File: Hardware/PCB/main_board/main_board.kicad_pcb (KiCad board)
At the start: 2 copper layers, 170 x 170 mm, 67 parts, among them J1 SWD, J2 USB_A, J3 DIN-5_180degree, J4 USB_B, J5 Conn_Coaxial, J6 AudioJack3, Q1 BC547, U1 MCP6002-xSN, U2 NUCLEO-F446RE, U3 6N137

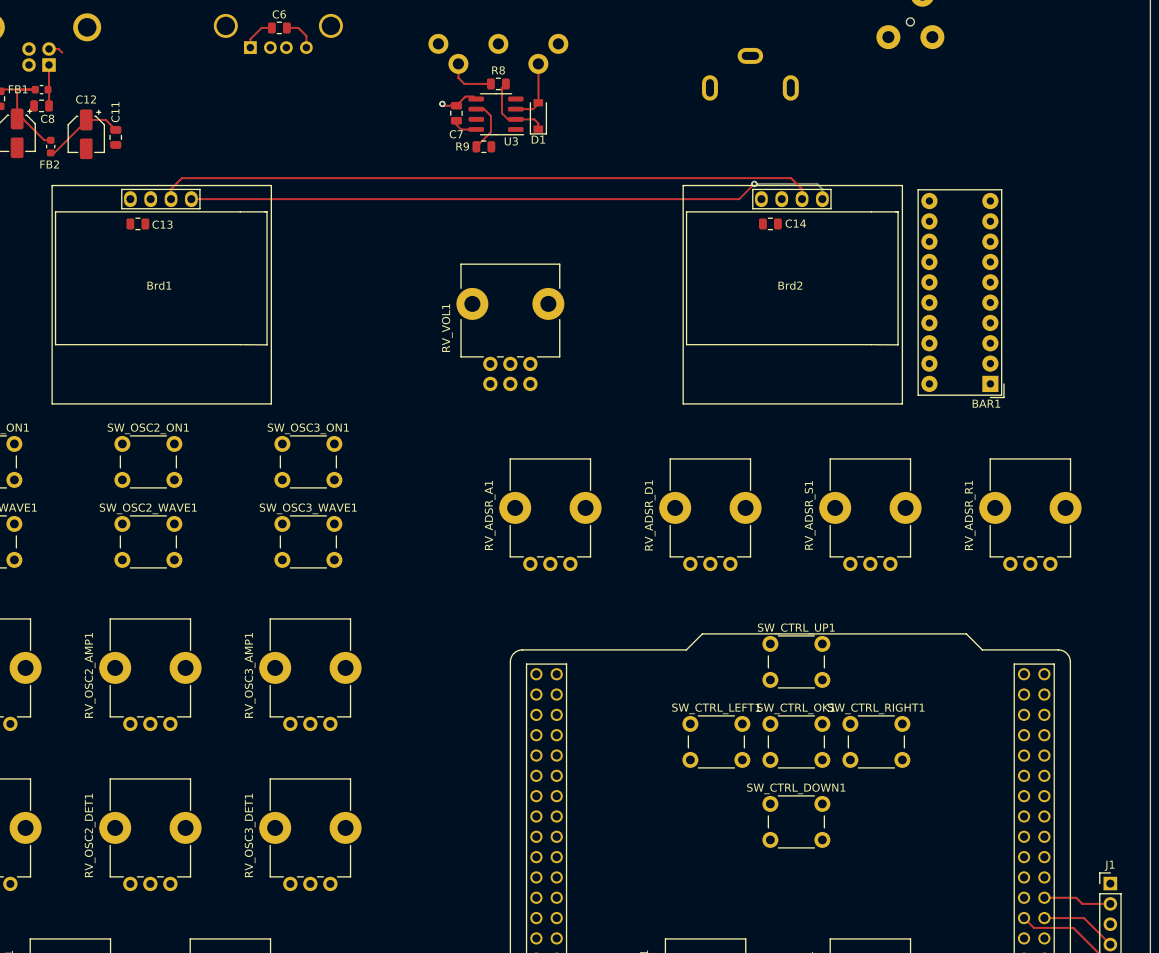
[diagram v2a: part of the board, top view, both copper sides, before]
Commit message: Update 3D view
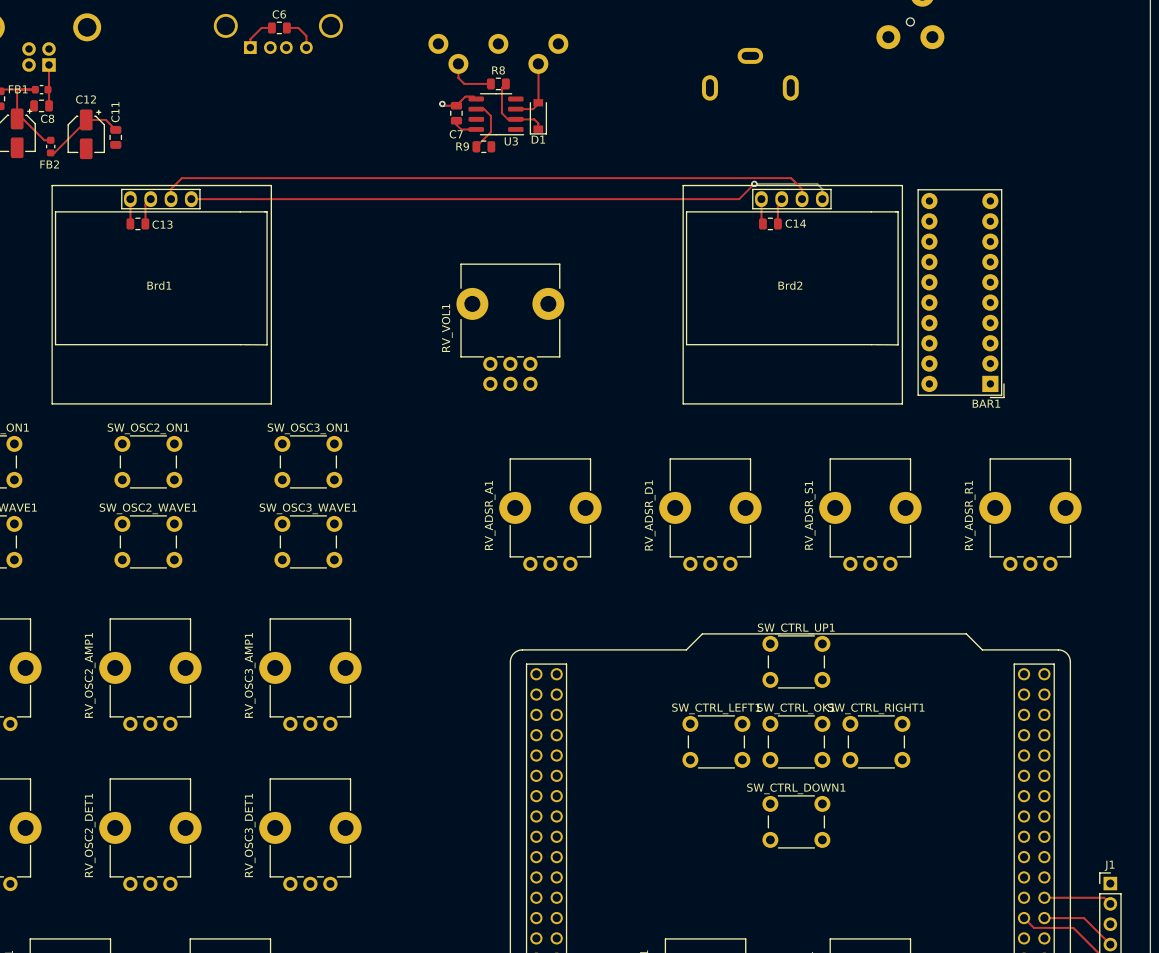
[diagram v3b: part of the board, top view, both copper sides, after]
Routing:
- net +5V: track 23.4 -> 30.1 mm
- net GND: track 22.1 -> 26.2 mm
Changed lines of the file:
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@@
     (thickness 1.6)
     (drawings 1)
-    (tracks 159)
+    (tracks 163)
     (zones 0)
     (modules 67)
@@
     (pad "" np_thru_hole circle (at 4 0 270) (size 1 1) (drill 1) (layers *.Cu *.Mask))
     (pad "" np_thru_hole circle (at 11.5 0 270) (size 1 1) (drill 1) (layers *.Cu *.Mask))
+    (model ${KIPRJMOD}/3dmodels/plastec_jack.stp
+      (offset (xyz 8 0 0))
+      (scale (xyz 0.85 0.9 0.6))
+      (rotate (xyz 0 0 180))
+    )
   )
   (module lib:MODULE_NUCLEO-F446RE (layer F.Cu)
@@
   (segment (start 72.0575 30.5) (end 73.5 30.5) (width 0.25) (layer F.Cu) (net 7))
   (segment (start 73.5 30.5) (end 74.5 31.5) (width 0.25) (layer F.Cu) (net 7))
-  (segment (start 43.529081 33.135) (end 44 33.605919) (width 0.25) (layer F.Cu) (net 7))
-  (segment (start 42.327 33.135) (end 43.529081 33.135) (width 0.25) (layer F.Cu) (net 7))
+  (segment (start 131.38 51.9) (end 131.38 54.8175) (width 0.25) (layer F.Cu) (net 7))
+  (segment (start 52.5 53.5) (end 52.5 55) (width 0.25) (layer F.Cu) (net 7))
+  (segment (start 52.5 51.9) (end 52.5 53.5) (width 0.25) (layer F.Cu) (net 7))
   (segment (start 89.176473 174.275027) (end 89.662 173.7895) (width 0.25) (layer F.Cu) (net 8))
   (segment (start 45 177.5) (end 47.5 180) (width 0.25) (layer F.Cu) (net 8))
@@
   (segment (start 171.69 141.77) (end 175 145.08) (width 0.25) (layer F.Cu) (net 71))
   (segment (start 166.75 141.77) (end 171.69 141.77) (width 0.25) (layer F.Cu) (net 71))
-  (segment (start 175 140) (end 171.5 140) (width 0.25) (layer F.Cu) (net 72))
-  (segment (start 170.73 139.23) (end 166.75 139.23) (width 0.25) (layer F.Cu) (net 72))
-  (segment (start 171.5 140) (end 170.73 139.23) (width 0.25) (layer F.Cu) (net 72))
+  (segment (start 174.23 139.23) (end 166.75 139.23) (width 0.25) (layer F.Cu) (net 72))
+  (segment (start 175 140) (end 174.23 139.23) (width 0.25) (layer F.Cu) (net 72))
   (segment (start 38.35 41.876) (end 38.35 38.215) (width 0.25) (layer F.Cu) (net 76))
   (segment (start 38.35 38.215) (end 40.6105 38.215) (width 0.25) (layer F.Cu) (net 76))
@@
   (segment (start 67.5 31.91) (end 68.91 30.5) (width 0.25) (layer F.Cu) (net 76))
   (segment (start 67.5 32.96) (end 67.5 31.91) (width 0.25) (layer F.Cu) (net 76))
+  (segment (start 133.4375 52.3825) (end 133.92 51.9) (width 0.25) (layer F.Cu) (net 76))
+  (segment (start 133.4375 55) (end 133.4375 52.3825) (width 0.25) (layer F.Cu) (net 76))
+  (segment (start 54.375 52.565) (end 55.04 51.9) (width 0.25) (layer F.Cu) (net 76))
+  (segment (start 54.375 55) (end 54.375 52.565) (width 0.25) (layer F.Cu) (net 76))
   (segment (start 103.5 34.99936) (end 103.49744 34.9968) (width 0.25) (layer F.Cu) (net 77))
   (segment (start 103.5 39.85) (end 103.5 34.99936) (width 0.25) (layer F.Cu) (net 77))

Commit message: Route GPIO
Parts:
- moved RV_LFO_RATE1 153.6 mm to (-83.1, 187.5)
- moved J1 148.8 mm to (28.0, 160.4)
- moved SW_CTRL_DOWN1 133.9 mm to (2.00, 157.5)
- moved SW_CTRL_LEFT1 133.9 mm to (-8.00, 147.5)
- moved SW_CTRL_OK1 133.9 mm to (2.00, 147.5)
- moved SW_CTRL_RIGHT1 133.9 mm to (12.0, 147.5)
- moved SW_CTRL_UP1 133.9 mm to (2.00, 137.5)
- moved BAR1 133.4 mm to (30.0, 105.0)
- moved Brd1 133.4 mm to (-73.9, 92.5)
- moved Brd2 133.4 mm to (5.00, 92.5)
- moved C1 133.4 mm to (-41.1, 194.2)
- moved C10 133.4 mm to (-91.7, 73.7)
- moved C11 133.4 mm to (-79.3, 74.2)
- moved C12 133.4 mm to (-83.0, 73.8)
- moved C13 133.4 mm to (-76.6, 85.0)
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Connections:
- net Net-(J4-Pad2) renamed /power/USB_B_D-
- net Net-(J4-Pad3) renamed /power/USB_B_D+
- net Net-(U2-PadCN10_16) renamed /MCU/MIDI_USB_VBUS
- net Net-(U2-PadCN10_21) renamed /MCU/MIDI_UART_TX
- J6 pad T: Net-(J6-PadT) -> Net-(J6-PadR)
- RV_ADSR_A1 pad 2: /HMI/ADSR_pot_A -> /MCU/ADC1_IN11
- RV_ADSR_D1 pad 2: /HMI/ADSR_pot_D -> /MCU/ADC1_IN10
- RV_ADSR_R1 pad 2: /HMI/ADSR_pot_R -> /MCU/ADC1_IN12
- RV_ADSR_S1 pad 2: /HMI/ADSR_pot_S -> /MCU/ADC1_IN13
- RV_LFO_DEPTH1 pad 2: /HMI/LFO_pot_DEPTH -> /MCU/ADC1_IN15
- RV_LFO_RATE1 pad 2: /HMI/LFO_pot_RATE -> /MCU/ADC1_IN6
- RV_OSC1_AMP1 pad 2: /HMI/OSC1_AMP -> /MCU/ADC1_IN2
- RV_OSC1_DET1 pad 2: /HMI/OSC1_DET -> /MCU/ADC1_IN14
- RV_OSC2_AMP1 pad 2: /HMI/OSC2_AMP -> /MCU/ADC1_IN3
- RV_OSC2_DET1 pad 2: /HMI/OSC2_DET -> /MCU/ADC1_IN9
- RV_OSC3_AMP1 pad 2: /HMI/OSC3_AMP -> /MCU/ADC1_IN8
- RV_OSC3_DET1 pad 2: /HMI/OSC3_DET -> /MCU/ADC1_IN7
- SW_CTRL_OK1 pad 2: /HMI/OSC2_OK -> /MCU/GPIO_PC15
- SW_OSC1_ON1 pad 2: /HMI/OSC1_ON -> /MCU/GPIO_PB4
- SW_OSC1_WAVE1 pad 2: /HMI/OSC1_WAVE -> /MCU/GPIO_PB14
- SW_OSC2_ON1 pad 2: /HMI/OSC2_ON -> /MCU/GPIO_PB15
- SW_OSC2_WAVE1 pad 2: /HMI/OSC2_WAVE -> /MCU/GPIO_PB5
- SW_OSC3_ON1 pad 2: /HMI/OSC3_ON -> /MCU/GPIO_PB10
- SW_OSC3_WAVE1 pad 2: /HMI/OSC3_WAVE -> /MCU/GPIO_PB13
- U2 pad CN10_12: Net-(U2-PadCN10_12) -> /MIDI/MIDI_USB_D+
- U2 pad CN10_13: Net-(U2-PadCN10_13) -> /MCU/ADC1_IN6
- U2 pad CN10_14: Net-(U2-PadCN10_14) -> /MIDI/MIDI_USB_D-
- U2 pad CN10_15: Net-(U2-PadCN10_15) -> /MCU/ADC1_IN7
- U2 pad CN10_17: Net-(U2-PadCN10_17) -> /HMI/I2C_display_SCL
- U2 pad CN10_24: Net-(U2-PadCN10_24) -> /MCU/ADC1_IN9
- U2 pad CN10_25: Net-(U2-PadCN10_25) -> /MCU/GPIO_PB10
- U2 pad CN10_26: Net-(U2-PadCN10_26) -> /MCU/GPIO_PB15
- U2 pad CN10_27: Net-(U2-PadCN10_27) -> /MCU/GPIO_PB4
- U2 pad CN10_28: Net-(U2-PadCN10_28) -> /MCU/GPIO_PB14
- U2 pad CN10_29: Net-(U2-PadCN10_29) -> /MCU/GPIO_PB5
- U2 pad CN10_30: Net-(U2-PadCN10_30) -> /MCU/GPIO_PB13
- U2 pad CN10_33: Net-(U2-PadCN10_33) -> /MIDI/MIDI_Serial_RX
- U2 pad CN10_34: Net-(U2-PadCN10_34) -> /MCU/ADC1_IN14
- U2 pad CN10_35: Net-(U2-PadCN10_35) -> /MCU/ADC1_IN2
- U2 pad CN10_37: Net-(U2-PadCN10_37) -> /MCU/ADC1_IN3
- U2 pad CN10_6: Net-(U2-PadCN10_6) -> /MCU/ADC1_IN15
- U2 pad CN7_21: Net-(U2-PadCN7_21) -> /HMI/I2C_display_SDA
- U2 pad CN7_23: Net-(U2-PadCN7_23) -> /HMI/CTRL_DOWN
- U2 pad CN7_25: Net-(U2-PadCN7_25) -> /HMI/CTRL_RIGHT
- U2 pad CN7_27: Net-(U2-PadCN7_27) -> /MCU/GPIO_PC15
- U2 pad CN7_28: Net-(U2-PadCN7_28) -> /HMI/CTRL_LEFT
- U2 pad CN7_30: Net-(U2-PadCN7_30) -> /HMI/CTRL_UP
- U2 pad CN7_34: Net-(U2-PadCN7_34) -> /MCU/ADC1_IN8
- U2 pad CN7_35: Net-(U2-PadCN7_35) -> /MCU/ADC1_IN12
- U2 pad CN7_36: Net-(U2-PadCN7_36) -> /MCU/ADC1_IN11
- U2 pad CN7_37: Net-(U2-PadCN7_37) -> /MCU/ADC1_IN13
- U2 pad CN7_38: Net-(U2-PadCN7_38) -> /MCU/ADC1_IN10
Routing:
- net /MIDI/MIDI_USB_D-: track 0.00 -> 120.7 mm, vias 0 -> 4
- net /MIDI/MIDI_USB_D+: track 0.00 -> 118.9 mm, vias 0 -> 3
- net /MCU/GPIO_PB4: track 0.00 -> 107.1 mm
- net /MCU/GPIO_PB14: track 0.00 -> 105.7 mm
- net /analogFX/AUDIO_IN: track 0.00 -> 105.6 mm, vias 0 -> 2
- net /HMI/I2C_display_SCL: track 82.5 -> 183.6 mm, vias 0 -> 2
- net /HMI/I2C_display_SDA: track 81.2 -> 178.8 mm
- net /MCU/ADC1_IN8: track 0.00 -> 96.4 mm, vias 0 -> 2
- net /MCU/ADC1_IN14: track 0.00 -> 96.4 mm
- net /MCU/GPIO_PB15: track 0.00 -> 93.2 mm
- net /MIDI/MIDI_Serial_RX: track 0.00 -> 81.0 mm, vias 0 -> 3
- net /MCU/ADC1_IN2: track 0.00 -> 79.1 mm
- net /MCU/GPIO_PB5: track 0.00 -> 79.0 mm
- net /MCU/GPIO_PB10: track 0.00 -> 73.0 mm
- net /MCU/ADC1_IN6: track 0.00 -> 71.8 mm
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
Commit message: Route PWR
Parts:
- added C15: 47p, Capacitor_SMD:C_0805_2012Metric, F.Cu at (101.8, 188.5)
- added C16: 1u, Capacitor_SMD:C_0805_2012Metric, F.Cu at (98.8, 186.0)
- added C17: 51p, Capacitor_SMD:C_0805_2012Metric, F.Cu at (98.8, 192.2)
- added C18: 220n, Capacitor_SMD:C_0805_2012Metric, F.Cu at (93.5, 187.2)
- added C19: 220n, Capacitor_SMD:C_0805_2012Metric, F.Cu at (154.5, 197.2)
- added C20: 100n, Capacitor_SMD:C_0805_2012Metric, F.Cu at (93.2, 195.2)
- added C21: 1u, Capacitor_SMD:C_0805_2012Metric, F.Cu at (87.2, 194.2)
- added D2: 1N4148W, Diode_SMD:D_SOD-123, F.Cu at (101.2, 192.2)
- added D3: 1N4148W, Diode_SMD:D_SOD-123, F.Cu at (104.0, 192.2)
- added G***: LOGO, lib:logo_INSA, F.Cu at (32.8, 203.0)
- added R10: 4.7k, Resistor_SMD:R_0805_2012Metric, F.Cu at (101.8, 186.2)
- added R11: 10k, Resistor_SMD:R_0805_2012Metric, F.Cu at (90.5, 186.0)
- added R12: 10k, Resistor_SMD:R_0805_2012Metric, F.Cu at (96.5, 186.0)
- added R13: 10k, Resistor_SMD:R_0805_2012Metric, F.Cu at (88.2, 186.0)
- added R14: 500, Resistor_SMD:R_0805_2012Metric, F.Cu at (104.8, 187.2)
- added R15: 1k, Resistor_SMD:R_0805_2012Metric, F.Cu at (96.0, 196.0)
- added R16: 220, Resistor_SMD:R_0805_2012Metric, F.Cu at (150.8, 197.2)
- added R17: 10k, Resistor_SMD:R_0805_2012Metric, F.Cu at (93.5, 185.0)
- added R18: 1k, Resistor_SMD:R_0805_2012Metric, F.Cu at (88.0, 191.2)
- added R19: 1k, Resistor_SMD:R_0805_2012Metric, F.Cu at (87.2, 196.5)
- added U4: RC4558, Package_SO:SOIC-8_3.9x4.9mm_P1.27mm, F.Cu at (93.2, 191.2)
- C5: value 4.7u -> 100n
- FB1, FB2: value BLM18pg221sn1d - Ferrite_Bead -> BLM21PG221SH1D - Ferrite_Bead; footprint Inductor_SMD:L_0603_1608Metric -> Inductor_SMD:L_0805_2012Metric
- RV_DIST_DRIVE1: value 10k -> 500k log
- RV_DIST_TONE1: value 10k -> 22k
- moved C8 143.9 mm to (55.2, 75.5), turned to 0 degrees
- moved BAR1 140.4 mm to (170.2, 112.2)
- moved Brd1 140.4 mm to (66.4, 99.8)
- moved Brd2 140.4 mm to (145.2, 99.8)
- moved C1 140.4 mm to (99.2, 201.5)
- moved C10 140.4 mm to (48.6, 80.9)
- moved C13 140.4 mm to (63.7, 92.2)
- moved C14 140.4 mm to (142.8, 92.2)
- moved C2 140.4 mm to (87.7, 208.1)
- moved C3 140.4 mm to (87.7, 211.9)
- moved C4 140.4 mm to (99.2, 203.5)
- moved C5 140.4 mm to (97.9, 209.3)
- moved C6 140.4 mm to (81.4, 67.8)
- moved C7 140.4 mm to (103.5, 78.4)
- moved C9 140.4 mm to (46.3, 76.6)
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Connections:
- net Net-(C8-Pad1) renamed /power/PWR_RAW
- C4 pad 1: /analogFX/AUDIO_OUT -> /analogFX/OUT_VCF__IN_DIST
- RV_DIST_DRIVE1 pad 2: Net-(RV_DIST_DRIVE1-Pad2) -> Net-(C17-Pad1)
- RV_DIST_DRIVE1 pad 3: Net-(RV_DIST_DRIVE1-Pad3) -> Net-(C17-Pad1)
- U2 pad CN10_20: Net-(U2-PadCN10_20) -> GND
- U2 pad CN10_32: Net-(U2-PadCN10_32) -> GND
- U2 pad CN10_9: Net-(U2-PadCN10_20) -> GND
- U2 pad CN7_19: Net-(U2-PadCN7_19) -> GND
- U2 pad CN7_20: Net-(U2-PadCN7_19) -> GND
- U2 pad CN7_22: Net-(U2-PadCN7_19) -> GND
- U2 pad CN7_6: Net-(U2-PadCN7_6) -> +5V
- U2 pad CN7_8: Net-(U2-PadCN7_19) -> GND
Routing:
- net +3V3: track 0.00 -> 299.5 mm, vias 0 -> 2
- net +5V: track 30.1 -> 322.8 mm, vias 0 -> 3
- net +5VA: track 18.9 -> 274.2 mm
- net Net-(C18-Pad1): track 0.00 -> 83.4 mm
- net /MCU/SWO: track 0.00 -> 73.4 mm, vias 0 -> 1
- net Net-(R18-Pad1): track 0.00 -> 66.6 mm, vias 0 -> 2
- net Net-(C17-Pad1): track 0.00 -> 41.6 mm
- net Net-(R14-Pad1): track 0.00 -> 39.3 mm
- net GND: track 26.2 -> 64.7 mm, vias 4 -> 12
- net /analogFX/OUT_VCF__IN_DIST: track 0.00 -> 34.2 mm, vias 0 -> 2
- net Net-(J2-Pad5): track 0.00 -> 16.0 mm
- net Net-(C15-Pad1): track 0.00 -> 13.6 mm
- net Net-(J4-Pad5): track 0.00 -> 12.0 mm
- net Net-(R11-Pad2): track 0.00 -> 10.1 mm
- net Net-(C16-Pad1): track 0.00 -> 8.01 mm
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- added copper zone on B.Cu, net GND
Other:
- net class GND added: clearance 0.2, trace_width 0.4, via_dia 0.9, via_drill 0.45
- net class Power added: clearance 0.2, trace_width 0.5, via_dia 1.2, via_drill 0.8
- rule via_min_size: 0.4 -> 0.45
